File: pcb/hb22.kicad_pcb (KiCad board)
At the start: 2 copper layers, 169 parts, among them J1 AVR-ISP-6, J10 ARK2500R-A-2P, J2 RJ12, J3 RJ12, J4 Conn_02x05, J5 15EDGRC-3.5-03P, J6 15EDGRC-3.5-03P, J7 ARK2500R-A-2P, J8 ARK2500R-A-2P, J9 5EDGRC-3.5-02P, Q1 BT148, Q10 IRFR5305, Q2 BC847, Q3 BC847, Q4 IRFR4105, Q5 BC817, Q6 IRFR4105, Q7 BC817, Q8 IRFR4105, Q9 IRFR4105, U1 74HC04, U10 LM75B, U11 TPS5430DDA, U12 LM75B, U13 INA219AxD, U14 LM78M05_TO252, U15 TL431DBZ, U16 TSV911IDT, U17 PC817, U18 LM75B, U2 74HC04, U3 74HC02, U4 74HC08, U5 74HC02, U6 ATmega328P-AU, U7 6N137, U8 PC817, U9 PC817, Y1 14.7456 MHz

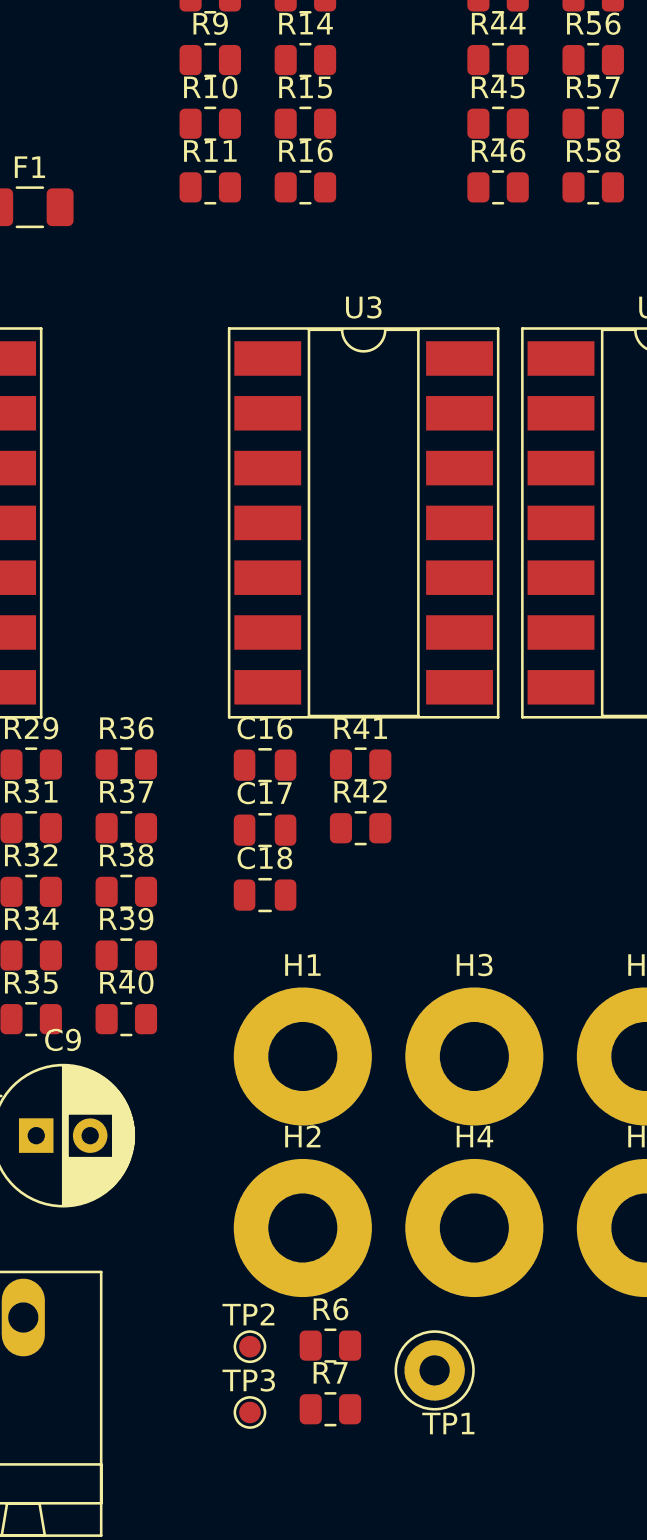
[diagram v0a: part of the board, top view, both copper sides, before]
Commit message: Bridge: use IRLR2905 transistors instead of IRFR4105.
IRFR4105 seem not to be available.
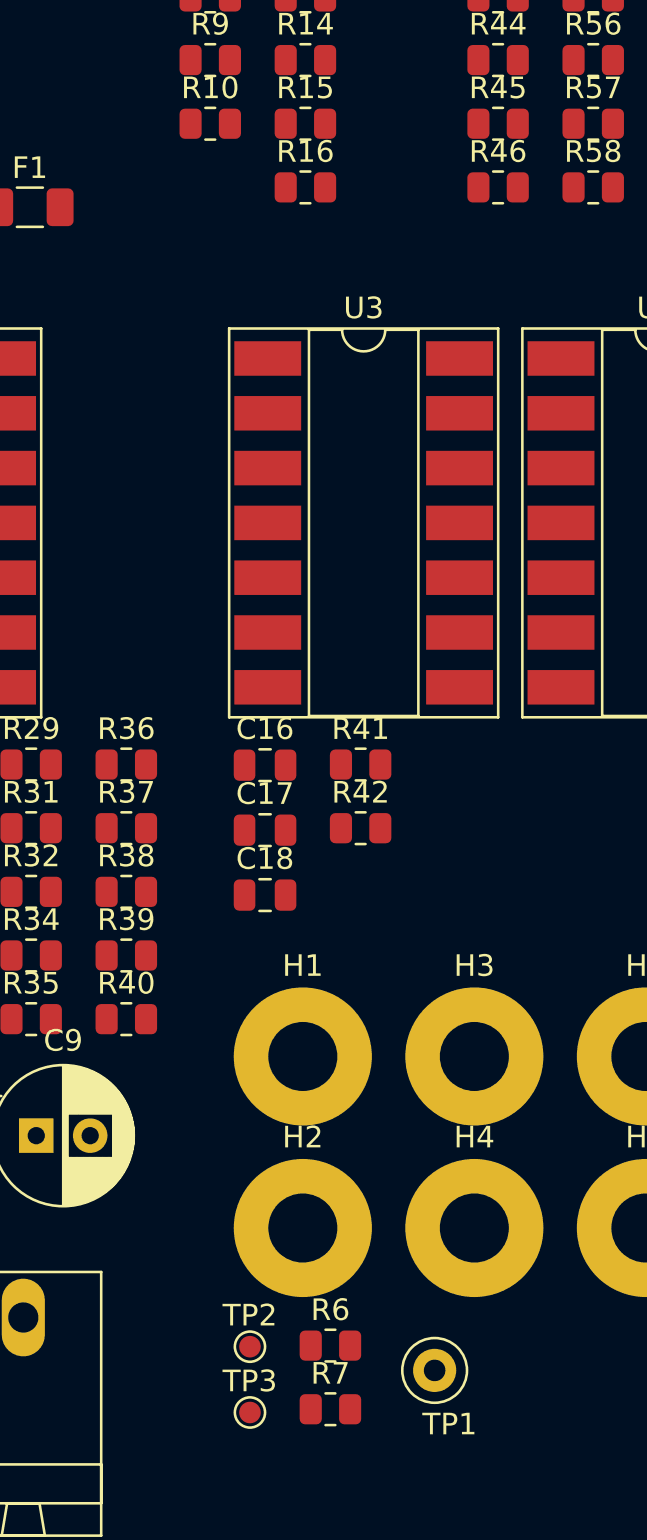
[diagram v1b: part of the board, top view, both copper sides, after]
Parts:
- removed R11: 250R, Resistor_SMD:R_0805_2012Metric
- Q4, Q6, Q8, Q9: value IRFR4105 -> IRLR2905
- R2: value 1k -> 10k
- TP1: footprint TestPoint:TestPoint_Loop_D3.50mm_Drill1.4mm_Beaded -> TestPoint:TestPoint_Loop_D1.80mm_Drill1.0mm_Beaded
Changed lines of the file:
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@@
 			)
 		)
-		(property "Value" "IRFR4105"
+		(property "Value" "IRLR2905"
 			(at 0 4.5 0)
 			(layer "F.Fab")
@@
 			)
 		)
-		(property "Value" "IRFR4105"
+		(property "Value" "IRLR2905"
 			(at 0 4.5 0)
 			(layer "F.Fab")
@@
 		)
 	)
-	(footprint "TestPoint:TestPoint_Loop_D3.50mm_Drill1.4mm_Beaded"
+	(footprint "TestPoint:TestPoint_Loop_D1.80mm_Drill1.0mm_Beaded"
 		(layer "F.Cu")
 		(at 181.370759 152.312)
-		(descr "wire loop with bead as test point, loop diameter 3.5mm, hole diameter 1.4mm")
+		(descr "wire loop with bead as test point, loop diameter 1.8mm, hole diameter 1.0mm")
 		(tags "test point wire loop bead")
 		(property "Reference" "TP1"
@@
 			)
 		)
-		(property "Footprint" "TestPoint:TestPoint_Loop_D3.50mm_Drill1.4mm_Beaded"
+		(property "Footprint" "TestPoint:TestPoint_Loop_D1.80mm_Drill1.0mm_Beaded"
 			(at 0 0 0)
 			(unlocked yes)
@@
 		(fp_circle
 			(center 0 0)
-			(end 1.8 0)
+			(end 1.5 0)
 			(stroke
 				(width 0.12)
@@
 		(fp_circle
 			(center 0 0)
-			(end 2.1 0)
+			(end 1.8 0)
 			(stroke
 				(width 0.05)
@@
 		)
 		(fp_line
-			(start -1.6 -0.3)
-			(end -1.6 0.3)
+			(start -0.9 -0.2)
+			(end 0.9 -0.2)
 			(stroke
 				(width 0.12)
@@
 		)
 		(fp_line
-			(start -1.6 0.3)
-			(end 1.6 0.3)
+			(start -0.9 0.2)
+			(end -0.9 -0.2)
 			(stroke
 				(width 0.12)
@@
 		)
 		(fp_line
-			(start 1.6 -0.3)
-			(end -1.6 -0.3)
+			(start 0.9 -0.2)
+			(end 0.9 0.2)
 			(stroke
 				(width 0.12)
@@
 		)
 		(fp_line
-			(start 1.6 0.3)
-			(end 1.6 -0.3)
+			(start 0.9 0.2)
+			(end -0.9 0.2)
 			(stroke
 				(width 0.12)
@@
 		(fp_circle
 			(center 0 0)
-			(end 1.5 0)
+			(end 1.3 0)
 			(stroke
 				(width 0.12)
@@
 		(pad "1" thru_hole circle
 			(at 0 0)
-			(size 2.8 2.8)
-			(drill 1.4)
+			(size 2 2)
+			(drill 1)
 			(layers "*.Cu" "*.Mask")
 			(remove_unused_layers no)
@@
 			(pintype "passive")
 		)
-		(model "${KICAD8_3DMODEL_DIR}/TestPoint.3dshapes/TestPoint_Loop_D3.50mm_Drill1.4mm_Beaded.wrl"
+		(model "${KICAD8_3DMODEL_DIR}/TestPoint.3dshapes/TestPoint_Loop_D1.80mm_Drill1.0mm_Beaded.wrl"
 			(offset
 				(xyz 0 0 0)
@@
 			)
 		)
-		(property "Value" "IRFR4105"
+		(property "Value" "IRLR2905"
 			(at 0 4.5 0)
 			(layer "F.Fab")
@@
 		)
 	)
-	(footprint "Resistor_SMD:R_0805_2012Metric"
-		(layer "F.Cu")
-		(at 170.970759 97.482)
-		(descr "Resistor SMD 0805 (2012 Metric), square (rectangular) end terminal, IPC_7351 nominal, (Body size source: IPC-SM-782 page 72, https://www.pcb-3d.com/wordpress/wp-content/uploads/ipc-sm-782a_amendment_1_and_2.pdf), generated with kicad-footprint-generator")
-		(tags "resistor")
-		(property "Reference" "R11"
-			(at 0 -1.65 0)
-			(layer "F.SilkS")
-			(effects
-				(font
-					(size 1 1)
-					(thickness 0.15)
-				)
-			)
-		)
-		(property "Value" "250R"
-			(at 0 1.65 0)
-			(layer "F.Fab")
-			(effects
-				(font
-					(size 1 1)
-					(thickness 0.15)
-				)
-			)
-		)
-		(property "Footprint" "Resistor_SMD:R_0805_2012Metric"
-			(at 0 0 0)
-			(unlocked yes)
-			(layer "F.Fab")
-			(hide yes)
-			(effects
-				(font
-					(size 1.27 1.27)
-					(thickness 0.15)
-				)
-			)
-		)
-		(property "Datasheet" ""
-			(at 0 0 0)
-			(unlocked yes)
-			(layer "F.Fab")
-			(hide yes)
-			(effects
-				(font
-					(size 1.27 1.27)
-					(thickness 0.15)
-				)
-			)
-		)
-		(property "Description" "Resistor"
-			(at 0 0 0)
-			(unlocked yes)
-			(layer "F.Fab")
-			(hide yes)
-			(effects
-				(font
-					(size 1.27 1.27)
-					(thickness 0.15)
-				)
-			)
-		)
-		(property ki_fp_filters "R_*")
-		(sheetname "IO")
-		(sheetfile "io.kicad_sch")
-		(attr smd)
-		(fp_line
-			(start -0.227064 -0.735)
-			(end 0.227064 -0.735)
-			(stroke
-				(width 0.12)
-				(type solid)
-			)
-			(layer "F.SilkS")
-		)
-		(fp_line
-			(start -0.227064 0.735)
-			(end 0.227064 0.735)
-			(stroke
-				(width 0.12)
-				(type solid)
-			)
-			(layer "F.SilkS")
-		)
-		(fp_line
-			(start -1.68 -0.95)
-			(end 1.68 -0.95)
-			(stroke
-				(width 0.05)
-				(type solid)
-			)
-			(layer "F.CrtYd")
-		)
-		(fp_line
-			(start -1.68 0.95)
-			(end -1.68 -0.95)
-			(stroke
-				(width 0.05)
-				(type solid)
-			)
-			(layer "F.CrtYd")
-		)
-		(fp_line
-			(start 1.68 -0.95)
-			(end 1.68 0.95)
-			(stroke
-				(width 0.05)
-				(type solid)
-			)
-			(layer "F.CrtYd")
-		)
-		(fp_line
-			(start 1.68 0.95)
-			(end -1.68 0.95)
-			(stroke
-				(width 0.05)
-				(type solid)
-			)
-			(layer "F.CrtYd")
-		)
-		(fp_line
-			(start -1 -0.625)
-			(end 1 -0.625)
-			(stroke
-				(width 0.1)
-				(type solid)
-			)
-			(layer "F.Fab")
-		)
-		(fp_line
-			(start -1 0.625)
-			(end -1 -0.625)
-			(stroke
-				(width 0.1)
-				(type solid)
-			)
-			(layer "F.Fab")
-		)
-		(fp_line
-			(start 1 -0.625)
-			(end 1 0.625)
-			(stroke
-				(width 0.1)
-				(type solid)
-			)
-			(layer "F.Fab")
-		)
-		(fp_line
-			(start 1 0.625)
-			(end -1 0.625)
-			(stroke
-				(width 0.1)
-				(type solid)
-			)
-			(layer "F.Fab")
-		)
-		(fp_text user "${REFERENCE}"
-			(at 0 0 0)
-			(layer "F.Fab")
-			(effects
-				(font
-					(size 0.5 0.5)
-					(thickness 0.08)
-				)
-			)
-		)
-		(pad "1" smd roundrect
-			(at -0.9125 0)
-			(size 1.025 1.4)
-			(layers "F.Cu" "F.Paste" "F.Mask")
-			(roundrect_rratio 0.243902)
-			(net 29 "Net-(J4-Pin_7)")
-			(pintype "passive")
-		)
-		(pad "2" smd roundrect
-			(at 0.9125 0)
-			(size 1.025 1.4)
-			(layers "F.Cu" "F.Paste" "F.Mask")
-			(roundrect_rratio 0.243902)
-			(net 88 "/B-TO-EXP")
-			(pintype "passive")
-		)
-		(model "${KICAD8_3DMODEL_DIR}/Resistor_SMD.3dshapes/R_0805_2012Metric.wrl"
-			(offset
-				(xyz 0 0 0)
-			)
-			(scale
-				(xyz 1 1 1)
-			)
-			(rotate
-				(xyz 0 0 0)
-			)
-		)
-	)
 	(footprint "Diode_SMD:D_SOD-123"
 		(layer "F.Cu")
@@
 			)
 		)
-		(property "Value" "1k"
+		(property "Value" "10k"
 			(at 0 1.65 0)
 			(layer "F.Fab")
@@
 			)
 		)
-		(property "Value" "IRFR4105"
+		(property "Value" "IRLR2905"
 			(at 0 4.5 0)
 			(layer "F.Fab")

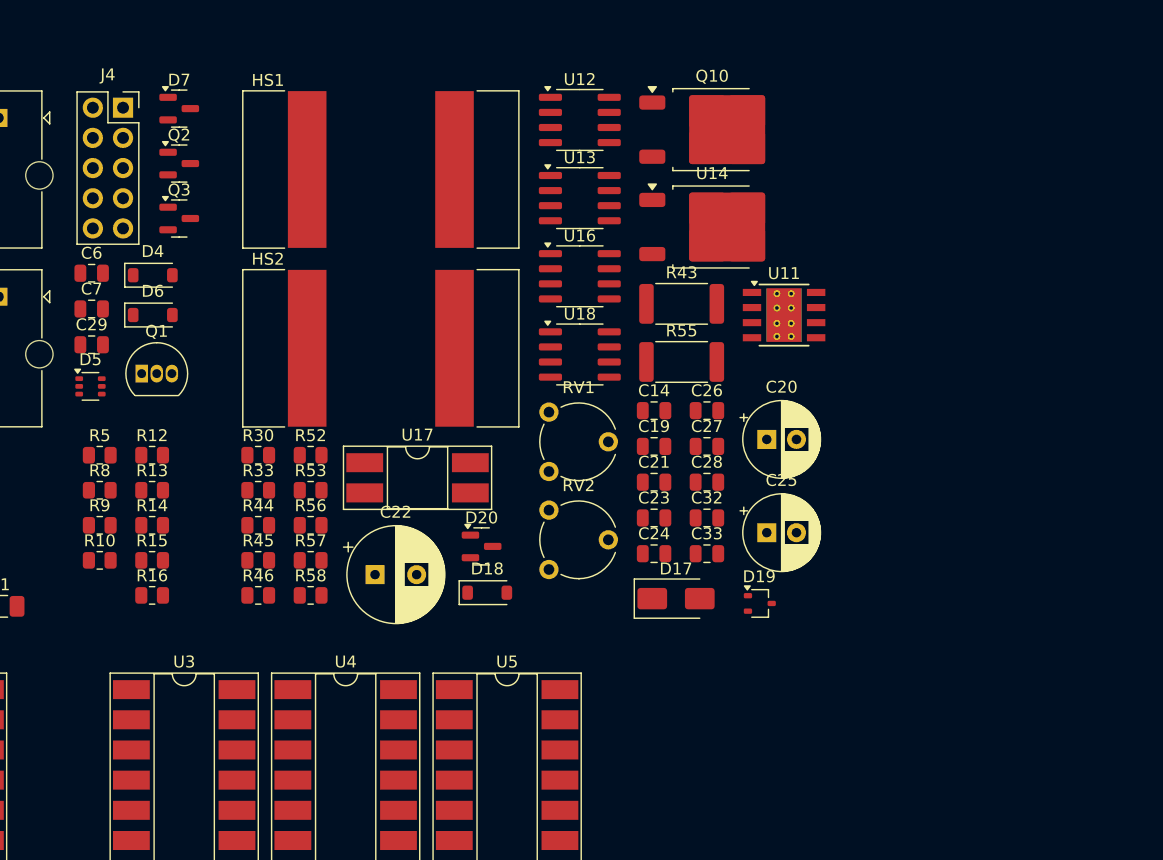
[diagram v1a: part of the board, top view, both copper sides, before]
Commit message: Add F5 missing footprint.
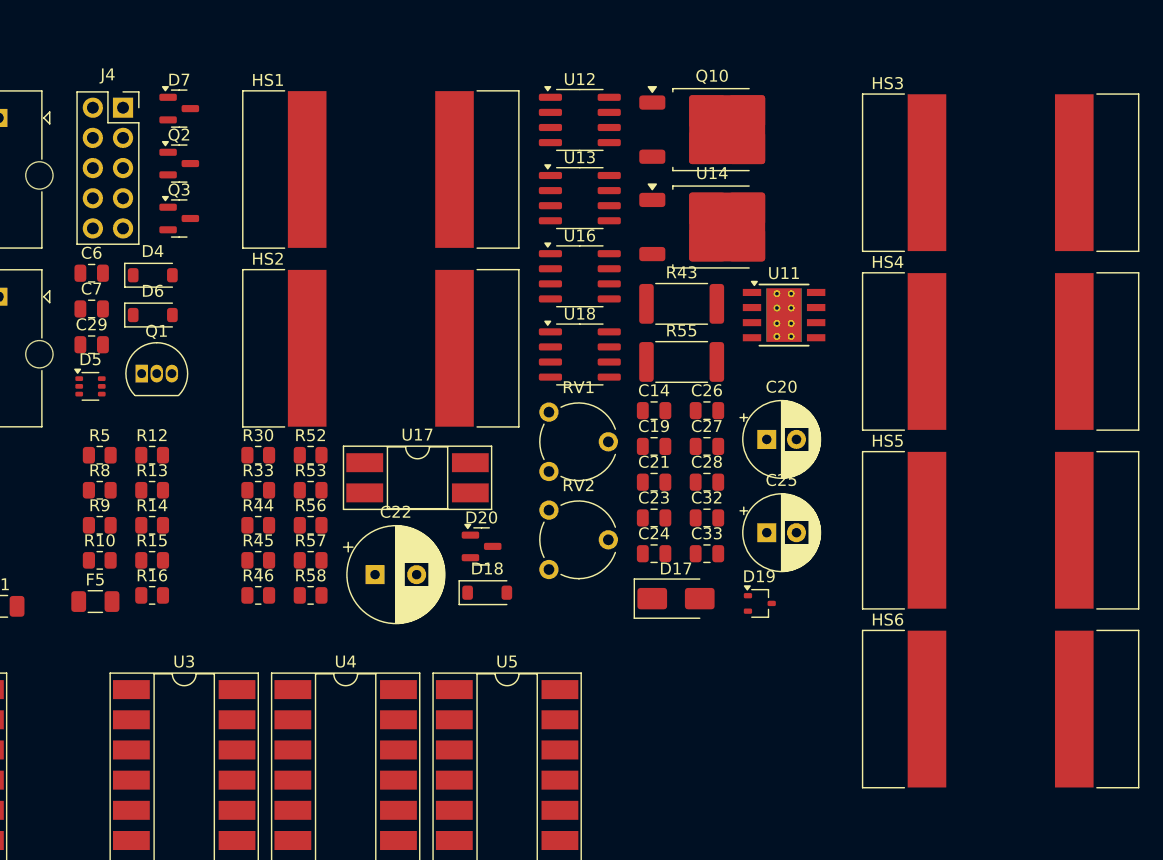
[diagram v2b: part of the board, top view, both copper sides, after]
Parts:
- added F5: 20 mA, Fuse:Fuse_1206_3216Metric, F.Cu at (170.6, 98.0)
- added HS3: FK24413, Heatsink:Heatsink_Fischer_FK24413DPAK_23x13mm, F.Cu at (246.8, 61.9)
- added HS4: FK24413, Heatsink:Heatsink_Fischer_FK24413DPAK_23x13mm, F.Cu at (246.8, 77.0)
- added HS5: FK24413, Heatsink:Heatsink_Fischer_FK24413DPAK_23x13mm, F.Cu at (246.8, 92.0)
- added HS6: FK24413, Heatsink:Heatsink_Fischer_FK24413DPAK_23x13mm, F.Cu at (246.8, 107.0)

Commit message: Use ATmega328pb instead of ATmega328p.
Reason: obtain some free pins as a reserve.
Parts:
- removed C25: 100u/35V, Capacitor_THT:CP_Radial_D6.3mm_P2.50mm
- removed C26: 100n, Capacitor_SMD:C_0805_2012Metric
- removed C27: 47u/6.3V, Capacitor_SMD:C_0805_2012Metric
- removed U14: LM78M05_TO252, Package_TO_SOT_SMD:TO-252-2
- added C30: 10n, Capacitor_SMD:C_0805_2012Metric, F.Cu at (379.0, 133.2)
- added C31: 100u/35V, Capacitor_THT:CP_Radial_D6.3mm_P2.50mm, F.Cu at (369.9, 145.1)
- added C34: 10u/35V, Capacitor_SMD:C_0805_2012Metric, F.Cu at (379.0, 136.2)
- added C35: 220u/6.3V, Capacitor_THT:CP_Radial_D8.0mm_P3.50mm, F.Cu at (370.3, 136.4)
- added C36: 100n, Capacitor_SMD:C_0805_2012Metric, F.Cu at (379.0, 139.2)
- added D22: SS54, Diode_SMD:D_SMA, F.Cu at (385.3, 140.6)
- added D23: BZX84C8V2, Package_TO_SOT_SMD:SOT-23, F.Cu at (379.8, 127.1)
- added F6: 300 mA, Fuse:Fuse_2920_7451Metric, F.Cu at (372.2, 128.2)
- added L2: 22uH, Inductor_SMD:L_Changjiang_FNR4020S, F.Cu at (384.1, 145.7)
- added R11: 10k, Resistor_SMD:R_0805_2012Metric, F.Cu at (379.0, 142.2)
- added R54: 10k, Resistor_SMD:R_0805_2012Metric, F.Cu at (379.0, 145.1)
- added R60: 3.24k, Resistor_SMD:R_0805_2012Metric, F.Cu at (379.0, 148.1)
- added U19: TPS5430DDA, Package_SO:TI_SO-PowerPAD-8_ThermalVias, F.Cu at (385.5, 135.1)
- D6: value !N5819 -> 1N5819
- D7: value BZX84C35 -> BZX84C33
- F1: value Polyfuse -> 100 mA
- Q1: footprint Package_TO_SOT_THT:TO-92_Inline -> Package_TO_SOT_SMD:SOT-223
- TP1: value TestPoint -> ring
- U6: value ATmega328P-AU -> ATmega328PB-AU
- moved C10 133.4 mm to (282.7, 133.2)
- moved C11 133.4 mm to (282.7, 136.2)
- moved C12 133.4 mm to (282.7, 139.3)
- moved C13 133.4 mm to (282.7, 142.3)
- moved C15 133.4 mm to (282.7, 145.3)
- moved C22 133.4 mm to (327.4, 101.7)
- moved C29 133.4 mm to (303.5, 82.3)
- moved C6 133.4 mm to (303.5, 76.3)
- moved C7 133.4 mm to (303.5, 79.3)
- moved C8 133.4 mm to (282.7, 130.2)
- moved D10 133.4 mm to (272.7, 133.8)
- moved D11 133.4 mm to (272.7, 137.1)
- moved D12 133.4 mm to (278.0, 131.1)
- moved D13 133.4 mm to (278.0, 135.8)
- moved D14 133.4 mm to (272.7, 140.4)
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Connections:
- U6 pad 3: GND -> unconnected-(U6-PE0-Pad3)
- U6 pad 6: +5V -> unconnected-(U6-PE1-Pad6)
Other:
- board outline added: 140 x 100 mm
- copper layers 2 -> 4
